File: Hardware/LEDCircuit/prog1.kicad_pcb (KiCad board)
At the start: 2 copper layers, 16 x 22 mm, 6 parts, among them J1 Conn_01x02, SW1 SW_Push

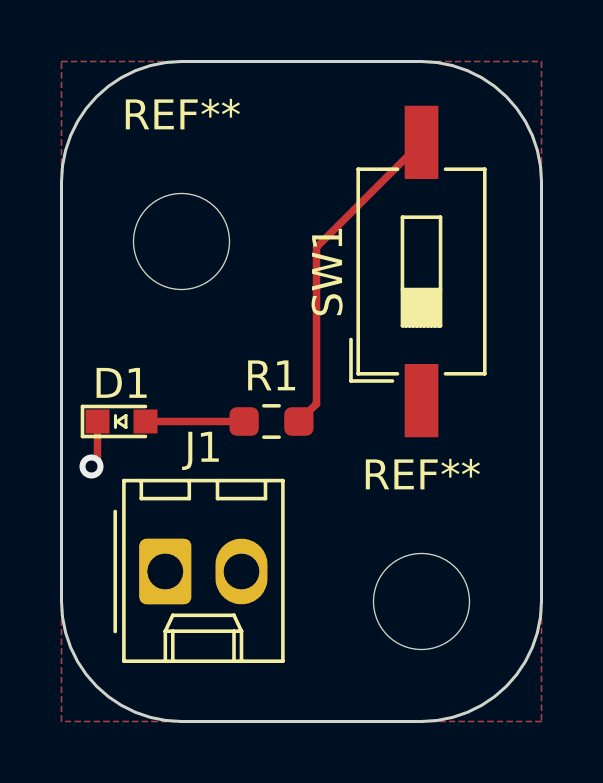
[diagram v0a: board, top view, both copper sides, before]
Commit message: Traces fixed for both hardware
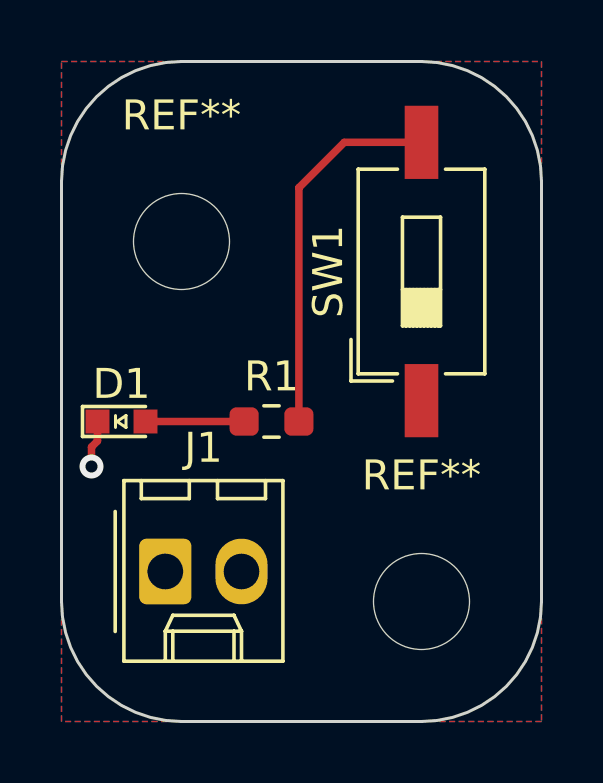
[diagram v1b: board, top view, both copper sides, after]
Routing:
- net Net-(R1-Pad1): track 11.0 -> 12.5 mm
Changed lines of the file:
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@@
 	)
 	(segment
-		(start 119.2 82.3)
+		(start 119 81.85)
 		(end 119 82.5)
 		(width 0.25)
@@
 	(segment
 		(start 119.2 81)
-		(end 119.2 82.3)
+		(end 119.2 81.65)
+		(width 0.25)
+		(layer "F.Cu")
+		(net 1)
+	)
+	(segment
+		(start 119.2 81.65)
+		(end 119 81.85)
 		(width 0.25)
 		(layer "F.Cu")
@@
 	)
 	(segment
-		(start 126.5 75.195)
-		(end 126.5 80.4125)
+		(start 125.9125 73.2075)
+		(end 127.425 71.695)
 		(width 0.25)
 		(layer "F.Cu")
@@
 	)
 	(segment
-		(start 130 71.695)
-		(end 126.5 75.195)
+		(start 125.9125 81)
+		(end 125.9125 73.2075)
 		(width 0.25)
 		(layer "F.Cu")
@@
 	)
 	(segment
-		(start 126.5 80.4125)
-		(end 125.9125 81)
+		(start 127.425 71.695)
+		(end 130 71.695)
 		(width 0.25)
 		(layer "F.Cu")
